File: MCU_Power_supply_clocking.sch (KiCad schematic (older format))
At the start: 114 parts, among them U6 STM32H743ZIT6, Y2 NX5032GA-8MHz, Y3 NX3215SA-32.768K-STD-MUA-14

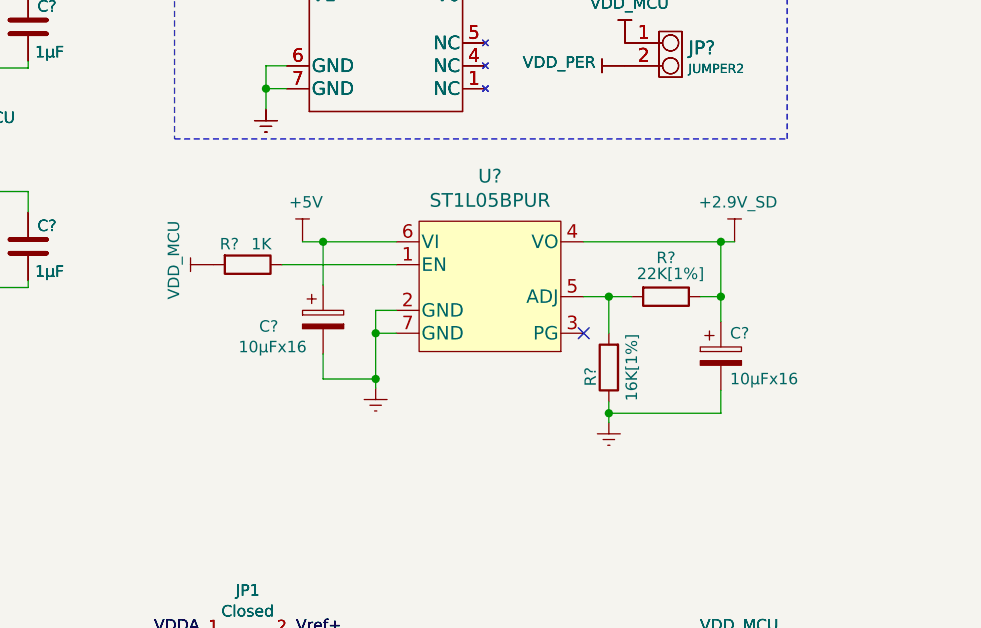
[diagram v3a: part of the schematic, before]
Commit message: 2.9V LDO changed
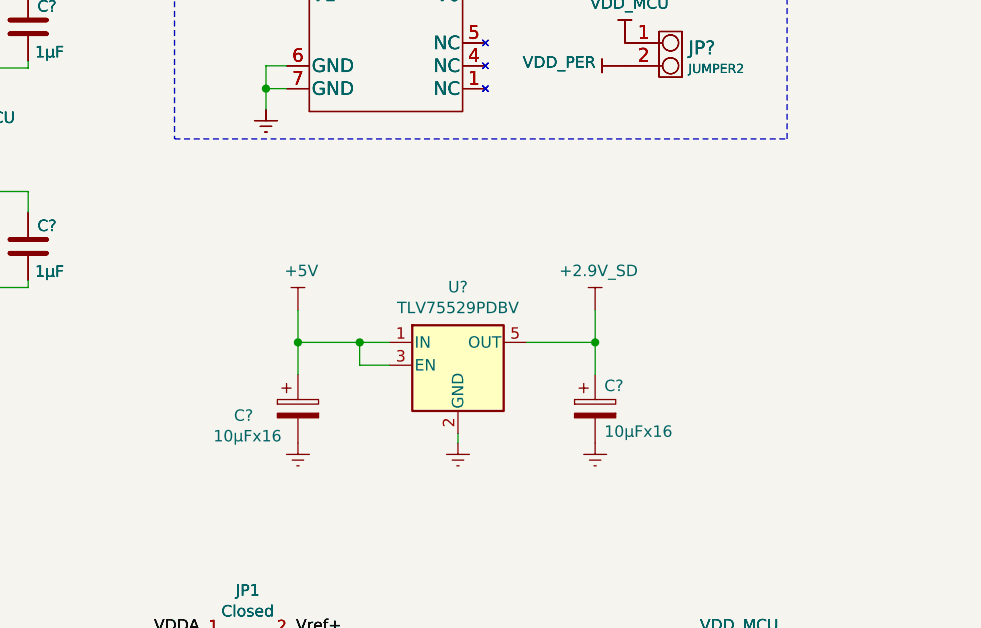
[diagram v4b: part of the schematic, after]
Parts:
- removed R?: 1K, Resistor_SMD:R_0805_2012Metric_Pad1.20x1.40mm_HandSolder, symbol Device:R
- removed R?: 22K[1%], Resistor_SMD:R_0805_2012Metric_Pad1.20x1.40mm_HandSolder, symbol Device:R
- removed R?: 16K[1%], Resistor_SMD:R_0805_2012Metric_Pad1.20x1.40mm_HandSolder, symbol Device:R
- removed U?: ST1L05BPUR, SVIELCOM:ST1L05BPUR, symbol SVIELCOM_Library:ST1L05BPUR
- added U?: TLV75529PDBV, Package_TO_SOT_SMD:SOT-23-5, symbol Regulator_Linear:TLV75529PDBV
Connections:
- net +2,9V: now also U?.5 (OUT)
- net +5V: now also U?.1 (IN), U?.3 (EN)
- net GNDREF: now also U?.2 (GND)
- no-connect marks 1 -> 0
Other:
- moved on the sheet: C?
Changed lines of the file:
@@
 $EndComp
-$Comp
-L SVIELCOM_Library:ST1L05BPUR U?
-U 1 1 6096844B
-P 8540 2460
-F 0 "U?" H 9150 2847 60  0000 C CNN
-F 1 "ST1L05BPUR" H 9150 2741 60  0000 C CNN
-F 2 "SVIELCOM:ST1L05BPUR" H 9110 2010 60  0001 C CNN
-F 3 "https://my.st.com/resource/en/datasheet/st1l05.pdf" H 9150 2741 60  0001 C CNN
-	1    8540 2460
-	1    0    0    -1
-$EndComp
-NoConn ~ 9560 2760
 $Comp
 L SVIELCOM_Library:+5V #PWR?
@@
 Backup LDO
 $Comp
-L power:GNDREF #PWR?
-U 1 1 60B41EE3
-P 8650 3000
-AR Path="/60B41EE3" Ref="#PWR?"  Part="1"
-AR Path="/60A03F8A/60B41EE3" Ref="#PWR?"  Part="1"
-F 0 "#PWR?" H 8650 2750 50  0001 C CNN
-F 1 "GNDREF" V 8655 2872 50  0001 R CNN
-F 2 "" H 8650 3000 50  0001 C CNN
-F 3 "" H 8650 3000 50  0001 C CNN
-	1    8650 3000
-	1    0    0    -1
-$EndComp
-Wire Wire Line
-	8650 3000 8650 2960
-Wire Wire Line
-	8650 2660 8740 2660
-Wire Wire Line
-	8740 2760 8650 2760
-Connection ~ 8650 2760
-Wire Wire Line
-	8650 2760 8650 2660
-$Comp
 L SVIELCOM_Library:+5V #PWR?
 U 1 1 60B6234A
-P 8330 2360
-F 0 "#PWR?" H 8330 2210 50  0001 C CNN
-F 1 "+5V" H 8345 2533 50  0000 C CNN
-F 2 "" H 8330 2360 50  0001 C CNN
-F 3 "" H 8330 2360 50  0001 C CNN
-	1    8330 2360
-	1    0    0    -1
-$EndComp
-$Comp
-L Device:R R?
-U 1 1 60B72F6C
-P 8090 2460
-AR Path="/60B72F6C" Ref="R?"  Part="1"
-AR Path="/60A03F8A/60B72F6C" Ref="R?"  Part="1"
-F 0 "R?" V 8000 2380 50  0000 C CNN
-F 1 "1K" V 8000 2520 50  0000 C CNN
-F 2 "Resistor_SMD:R_0805_2012Metric_Pad1.20x1.40mm_HandSolder" V 8020 2460 50  0001 C CNN
-F 3 "~" H 8090 2460 50  0001 C CNN
-	1    8090 2460
-	0    1    1    0
+P 8310 2660
+F 0 "#PWR?" H 8310 2510 50  0001 C CNN
+F 1 "+5V" H 8325 2833 50  0000 C CNN
+F 2 "" H 8310 2660 50  0001 C CNN
+F 3 "" H 8310 2660 50  0001 C CNN
+	1    8310 2660
+	1    0    0    -1
 $EndComp
 $Comp
 L Device:CP C?
 U 1 1 60B74100
-P 8420 2700
+P 8310 3090
 AR Path="/60B74100" Ref="C?"  Part="1"
 AR Path="/60A03F8A/60B74100" Ref="C?"  Part="1"
-F 0 "C?" H 8140 2670 50  0000 L CNN
-F 1 "10µFx16" H 8050 2580 50  0000 L CNN
-F 2 "" H 8458 2550 50  0001 C CNN
-F 3 "" H 8420 2700 50  0001 C CNN
-F 4 "593D106X9016A2TE3" H 8420 2700 50  0001 C CNN "Type"
-	1    8420 2700
-	1    0    0    -1
-$EndComp
-$Comp
-L SVIELCOM_Library:VDD_MCU #PWR?
-U 1 1 60BA614F
-P 7940 2460
-AR Path="/60BA614F" Ref="#PWR?"  Part="1"
-AR Path="/60A03F8A/60BA614F" Ref="#PWR?"  Part="1"
-F 0 "#PWR?" H 7940 2310 50  0001 C CNN
-F 1 "VDD_MCU" H 7960 2633 50  0000 C CNN
-F 2 "" H 7940 2460 50  0001 C CNN
-F 3 "" H 7940 2460 50  0001 C CNN
-	1    7940 2460
-	0    -1   -1   0
-$EndComp
-Wire Wire Line
-	8240 2460 8740 2460
-$Comp
-L Device:R R?
-U 1 1 60BBA878
-P 9920 2600
-AR Path="/60BBA878" Ref="R?"  Part="1"
-AR Path="/60A03F8A/60BBA878" Ref="R?"  Part="1"
-F 0 "R?" V 9750 2600 50  0000 C CNN
-F 1 "22K[1%]" V 9820 2620 50  0000 C CNN
-F 2 "Resistor_SMD:R_0805_2012Metric_Pad1.20x1.40mm_HandSolder" V 9850 2600 50  0001 C CNN
-F 3 "~" H 9920 2600 50  0001 C CNN
-	1    9920 2600
-	0    1    1    0
-$EndComp
-$Comp
-L Device:R R?
-U 1 1 60BBB173
-P 9670 2910
-AR Path="/60BBB173" Ref="R?"  Part="1"
-AR Path="/60A03F8A/60BBB173" Ref="R?"  Part="1"
-F 0 "R?" V 9750 2950 50  0000 C CNN
-F 1 "16K[1%]" V 9570 2910 50  0000 C CNN
-F 2 "Resistor_SMD:R_0805_2012Metric_Pad1.20x1.40mm_HandSolder" V 9600 2910 50  0001 C CNN
-F 3 "~" H 9670 2910 50  0001 C CNN
-	1    9670 2910
-	-1   0    0    1
-$EndComp
-Wire Wire Line
-	9560 2600 9670 2600
-Wire Wire Line
-	9670 2760 9670 2600
-Connection ~ 9670 2600
-Wire Wire Line
-	9670 2600 9770 2600
+F 0 "C?" H 8030 3060 50  0000 L CNN
+F 1 "10µFx16" H 7940 2970 50  0000 L CNN
+F 2 "" H 8348 2940 50  0001 C CNN
+F 3 "" H 8310 3090 50  0001 C CNN
+F 4 "593D106X9016A2TE3" H 8310 3090 50  0001 C CNN "Type"
+	1    8310 3090
+	1    0    0    -1
+$EndComp
 $Comp
 L power:GNDREF #PWR?
 U 1 1 60BED935
-P 9670 3150
+P 9010 3240
 AR Path="/60BED935" Ref="#PWR?"  Part="1"
 AR Path="/60A03F8A/60BED935" Ref="#PWR?"  Part="1"
-F 0 "#PWR?" H 9670 2900 50  0001 C CNN
-F 1 "GNDREF" V 9675 3022 50  0001 R CNN
-F 2 "" H 9670 3150 50  0001 C CNN
-F 3 "" H 9670 3150 50  0001 C CNN
-	1    9670 3150
-	1    0    0    -1
-$EndComp
-Wire Wire Line
-	9670 3150 9670 3110
-Wire Wire Line
-	9560 2360 10160 2360
-Wire Wire Line
-	10160 2360 10160 2600
-Wire Wire Line
-	10160 2600 10070 2600
+F 0 "#PWR?" H 9010 2990 50  0001 C CNN
+F 1 "GNDREF" V 9015 3112 50  0001 R CNN
+F 2 "" H 9010 3240 50  0001 C CNN
+F 3 "" H 9010 3240 50  0001 C CNN
+	1    9010 3240
+	1    0    0    -1
+$EndComp
 $Comp
 L Device:CP C?
 U 1 1 60C10398
-P 10160 2860
+P 9610 3090
 AR Path="/60C10398" Ref="C?"  Part="1"
 AR Path="/60A03F8A/60C10398" Ref="C?"  Part="1"
-F 0 "C?" H 10200 2960 50  0000 L CNN
-F 1 "10µFx16" H 10200 2760 50  0000 L CNN
-F 2 "" H 10198 2710 50  0001 C CNN
-F 3 "" H 10160 2860 50  0001 C CNN
-F 4 "593D106X9016A2TE3" H 10160 2860 50  0001 C CNN "Type"
-	1    10160 2860
-	1    0    0    -1
-$EndComp
-Wire Wire Line
-	10160 2710 10160 2600
-Connection ~ 10160 2600
-Wire Wire Line
-	9670 3110 10160 3110
-Wire Wire Line
-	10160 3110 10160 3010
-Connection ~ 9670 3110
-Wire Wire Line
-	9670 3110 9670 3060
+F 0 "C?" H 9650 3190 50  0000 L CNN
+F 1 "10µFx16" H 9650 2990 50  0000 L CNN
+F 2 "" H 9648 2940 50  0001 C CNN
+F 3 "" H 9610 3090 50  0001 C CNN
+F 4 "593D106X9016A2TE3" H 9610 3090 50  0001 C CNN "Type"
+	1    9610 3090
+	1    0    0    -1
+$EndComp
 $Comp
 L SVIELCOM_Library:+2.9V_SD #PWR?
 U 1 1 60C4B601
-P 10220 2360
-F 0 "#PWR?" H 10220 2210 50  0001 C CNN
-F 1 "+2.9V_SD" H 10235 2533 50  0000 C CNN
-F 2 "" H 10220 2360 50  0001 C CNN
-F 3 "" H 10220 2360 50  0001 C CNN
-	1    10220 2360
-	1    0    0    -1
-$EndComp
-Wire Wire Line
-	10160 2360 10220 2360
-Connection ~ 10160 2360
-Wire Wire Line
-	8330 2360 8420 2360
-Wire Wire Line
-	8420 2550 8420 2360
-Connection ~ 8420 2360
-Wire Wire Line
-	8420 2360 8740 2360
-Wire Wire Line
-	8420 2960 8650 2960
-Connection ~ 8650 2960
-Wire Wire Line
-	8650 2960 8650 2760
-Wire Wire Line
-	8420 2850 8420 2960
+P 9610 2660
+F 0 "#PWR?" H 9610 2510 50  0001 C CNN
+F 1 "+2.9V_SD" H 9625 2833 50  0000 C CNN
+F 2 "" H 9610 2660 50  0001 C CNN
+F 3 "" H 9610 2660 50  0001 C CNN
+	1    9610 2660
+	1    0    0    -1
+$EndComp
 $Comp
 L freetronics_schematic:JUMPER2 JP?
@@
 	0    -1   -1   0
 $EndComp
+$Comp
+L Regulator_Linear:TLV75529PDBV U?
+U 1 1 60A1589A
+P 9010 2900
+F 0 "U?" H 9010 3242 50  0000 C CNN
+F 1 "TLV75529PDBV" H 9010 3151 50  0000 C CNN
+F 2 "Package_TO_SOT_SMD:SOT-23-5" H 9010 3225 50  0001 C CIN
+F 3 "http://www.ti.com/lit/ds/symlink/tlv755p.pdf" H 9010 2950 50  0001 C CNN
+	1    9010 2900
+	1    0    0    -1
+$EndComp
+Wire Wire Line
+	8310 2660 8310 2800
+Wire Wire Line
+	8710 2900 8580 2900
+Wire Wire Line
+	8580 2900 8580 2800
+Wire Wire Line
+	8580 2800 8310 2800
+Connection ~ 8310 2800
+Wire Wire Line
+	8310 2800 8310 2940
+Wire Wire Line
+	8580 2800 8710 2800
+Connection ~ 8580 2800
+Wire Wire Line
+	9310 2800 9610 2800
+Wire Wire Line
+	9610 2800 9610 2660
+Connection ~ 9610 2800
+Wire Wire Line
+	9610 2800 9610 2940
+$Comp
+L power:GNDREF #PWR?
+U 1 1 60A8F4E3
+P 8310 3240
+AR Path="/60A8F4E3" Ref="#PWR?"  Part="1"
+AR Path="/60A03F8A/60A8F4E3" Ref="#PWR?"  Part="1"
+F 0 "#PWR?" H 8310 2990 50  0001 C CNN
+F 1 "GNDREF" V 8315 3112 50  0001 R CNN
+F 2 "" H 8310 3240 50  0001 C CNN
+F 3 "" H 8310 3240 50  0001 C CNN
+	1    8310 3240
+	1    0    0    -1
+$EndComp
+$Comp
+L power:GNDREF #PWR?
+U 1 1 60A8FAA0
+P 9610 3240
+AR Path="/60A8FAA0" Ref="#PWR?"  Part="1"
+AR Path="/60A03F8A/60A8FAA0" Ref="#PWR?"  Part="1"
+F 0 "#PWR?" H 9610 2990 50  0001 C CNN
+F 1 "GNDREF" V 9615 3112 50  0001 R CNN
+F 2 "" H 9610 3240 50  0001 C CNN
+F 3 "" H 9610 3240 50  0001 C CNN
+	1    9610 3240
+	1    0    0    -1
+$EndComp
+Wire Wire Line
+	9010 3240 9010 3200
 $EndSCHEMATC
